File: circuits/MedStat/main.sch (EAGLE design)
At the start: 13 parts, among them U1 BLE113-VISUAL-A, U2 MMA8452Q

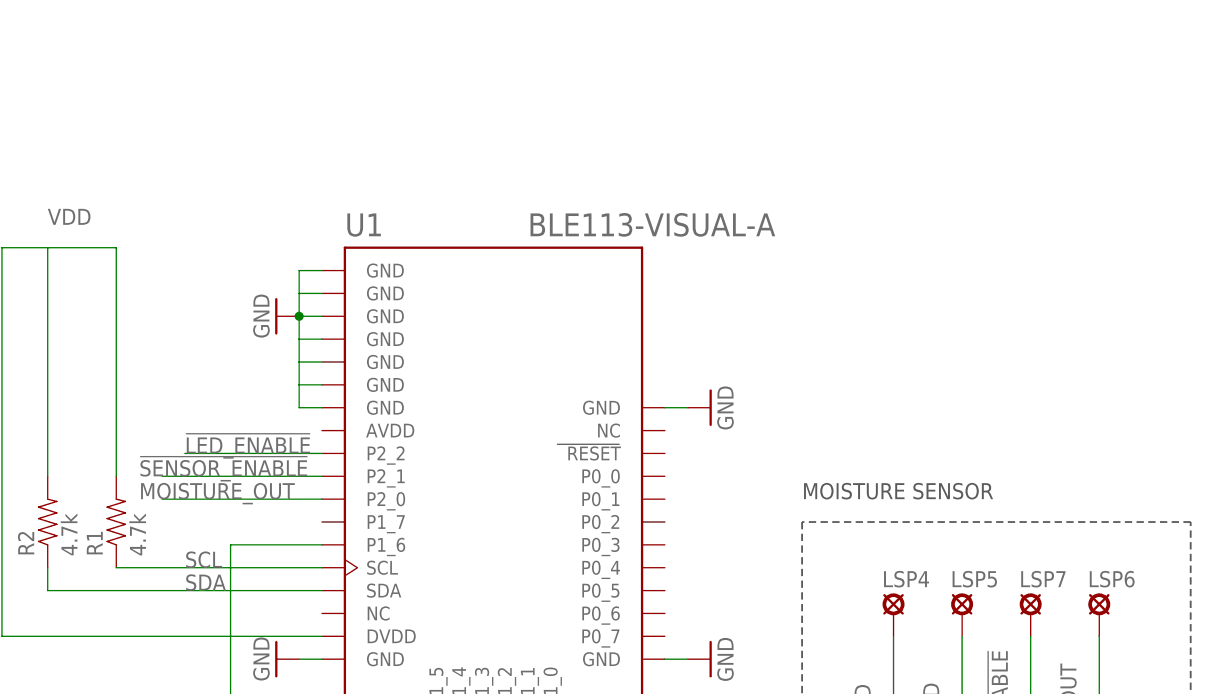
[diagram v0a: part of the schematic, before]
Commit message: Added pulse sensor ports
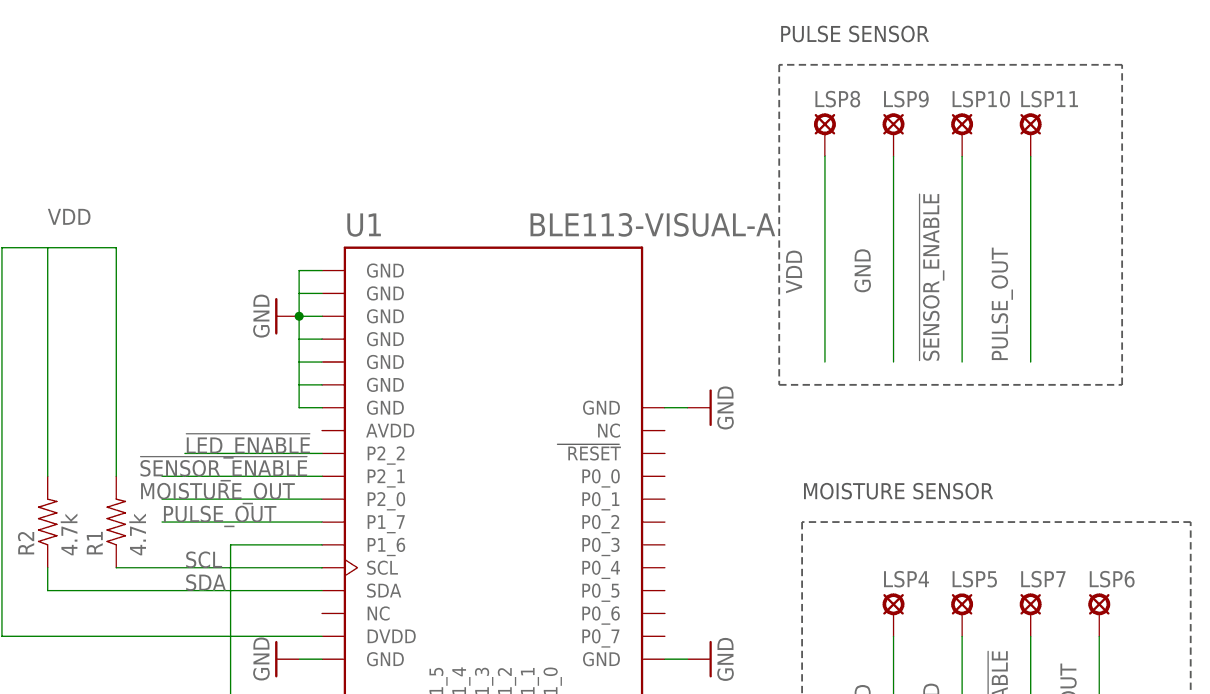
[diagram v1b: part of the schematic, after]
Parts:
- added LSP10, LSP11, LSP8, LSP9: LSP10, solpad:LSP10
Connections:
- new net PULSE_OUT: LSP11.MP, U1.P1_7
- net !SENSOR_ENABLE: now also LSP10.MP
- net GND: now also LSP9.MP
- net VDD: now also LSP8.MP
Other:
- note added: "PULSE SENSOR"
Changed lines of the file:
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@@
 <part name="LSP6" library="solpad" deviceset="LSP10" device=""/>
 <part name="LSP7" library="solpad" deviceset="LSP10" device=""/>
+<part name="LSP8" library="solpad" deviceset="LSP10" device=""/>
+<part name="LSP9" library="solpad" deviceset="LSP10" device=""/>
+<part name="LSP10" library="solpad" deviceset="LSP10" device=""/>
+<part name="LSP11" library="solpad" deviceset="LSP10" device=""/>
 </parts>
 <sheets>
@@
 <wire x1="76.2" y1="-2.54" x2="33.02" y2="-2.54" width="0.2032" layer="97" style="shortdash"/>
 <text x="33.02" y="0" size="1.778" layer="97">MOISTURE SENSOR</text>
+<wire x1="30.48" y1="48.26" x2="30.48" y2="12.7" width="0.2032" layer="97" style="shortdash"/>
+<wire x1="30.48" y1="12.7" x2="68.58" y2="12.7" width="0.2032" layer="97" style="shortdash"/>
+<wire x1="68.58" y1="12.7" x2="68.58" y2="48.26" width="0.2032" layer="97" style="shortdash"/>
+<wire x1="68.58" y1="48.26" x2="30.48" y2="48.26" width="0.2032" layer="97" style="shortdash"/>
+<text x="30.48" y="50.8" size="1.778" layer="97">PULSE SENSOR</text>
 </plain>
 <instances>
@@
 <instance part="LSP6" gate="1" x="66.04" y="-12.7"/>
 <instance part="LSP7" gate="1" x="58.42" y="-12.7"/>
+<instance part="LSP8" gate="1" x="35.56" y="40.64"/>
+<instance part="LSP9" gate="1" x="43.18" y="40.64"/>
+<instance part="LSP10" gate="1" x="50.8" y="40.64"/>
+<instance part="LSP11" gate="1" x="58.42" y="40.64"/>
 </instances>
 <busses>
@@
 <label x="48.26" y="-25.4" size="1.778" layer="95" rot="R90"/>
 </segment>
+<segment>
+<pinref part="LSP9" gate="1" pin="MP"/>
+<wire x1="43.18" y1="38.1" x2="43.18" y2="15.24" width="0.2032" layer="91"/>
+<label x="40.64" y="22.86" size="1.778" layer="95" rot="R90"/>
+</segment>
 </net>
 <net name="SDA" class="0">
@@
 <label x="40.64" y="-25.4" size="1.778" layer="95" rot="R90"/>
 </segment>
+<segment>
+<pinref part="LSP8" gate="1" pin="MP"/>
+<wire x1="35.56" y1="38.1" x2="35.56" y2="15.24" width="0.2032" layer="91"/>
+<label x="33.02" y="22.86" size="1.778" layer="95" rot="R90"/>
+</segment>
 </net>
 <net name="!LED_ENABLE" class="0">
@@
 <label x="-40.64" y="2.54" size="1.778" layer="95"/>
 </segment>
+<segment>
+<pinref part="LSP10" gate="1" pin="MP"/>
+<wire x1="50.8" y1="38.1" x2="50.8" y2="15.24" width="0.2032" layer="91"/>
+<label x="48.26" y="15.24" size="1.778" layer="95" rot="R90"/>
+</segment>
 </net>
 <net name="MOISTURE_OUT" class="0">
@@
 </segment>
 </net>
+<net name="PULSE_OUT" class="0">
+<segment>
+<pinref part="LSP11" gate="1" pin="MP"/>
+<wire x1="58.42" y1="38.1" x2="58.42" y2="15.24" width="0.2032" layer="91"/>
+<label x="55.88" y="15.24" size="1.778" layer="95" rot="R90"/>
+</segment>
+<segment>
+<pinref part="U1" gate="G$1" pin="P1_7"/>
+<wire x1="-20.32" y1="-2.54" x2="-38.1" y2="-2.54" width="0.2032" layer="91"/>
+<label x="-38.1" y="-2.54" size="1.778" layer="95"/>
+</segment>
+</net>

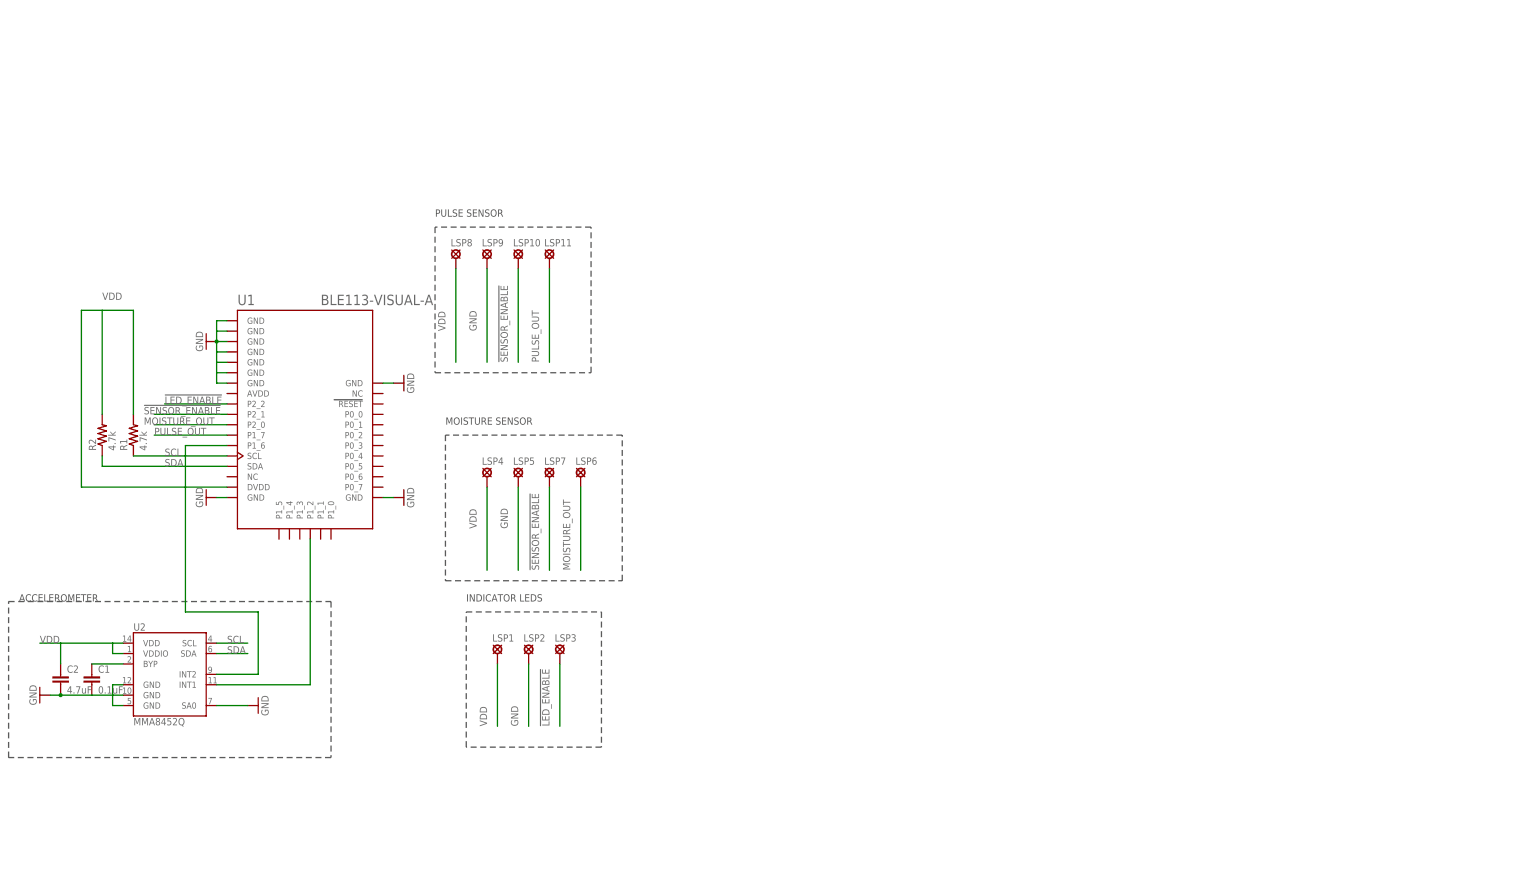
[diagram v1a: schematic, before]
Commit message: Integrated EPD driver to main schematic.
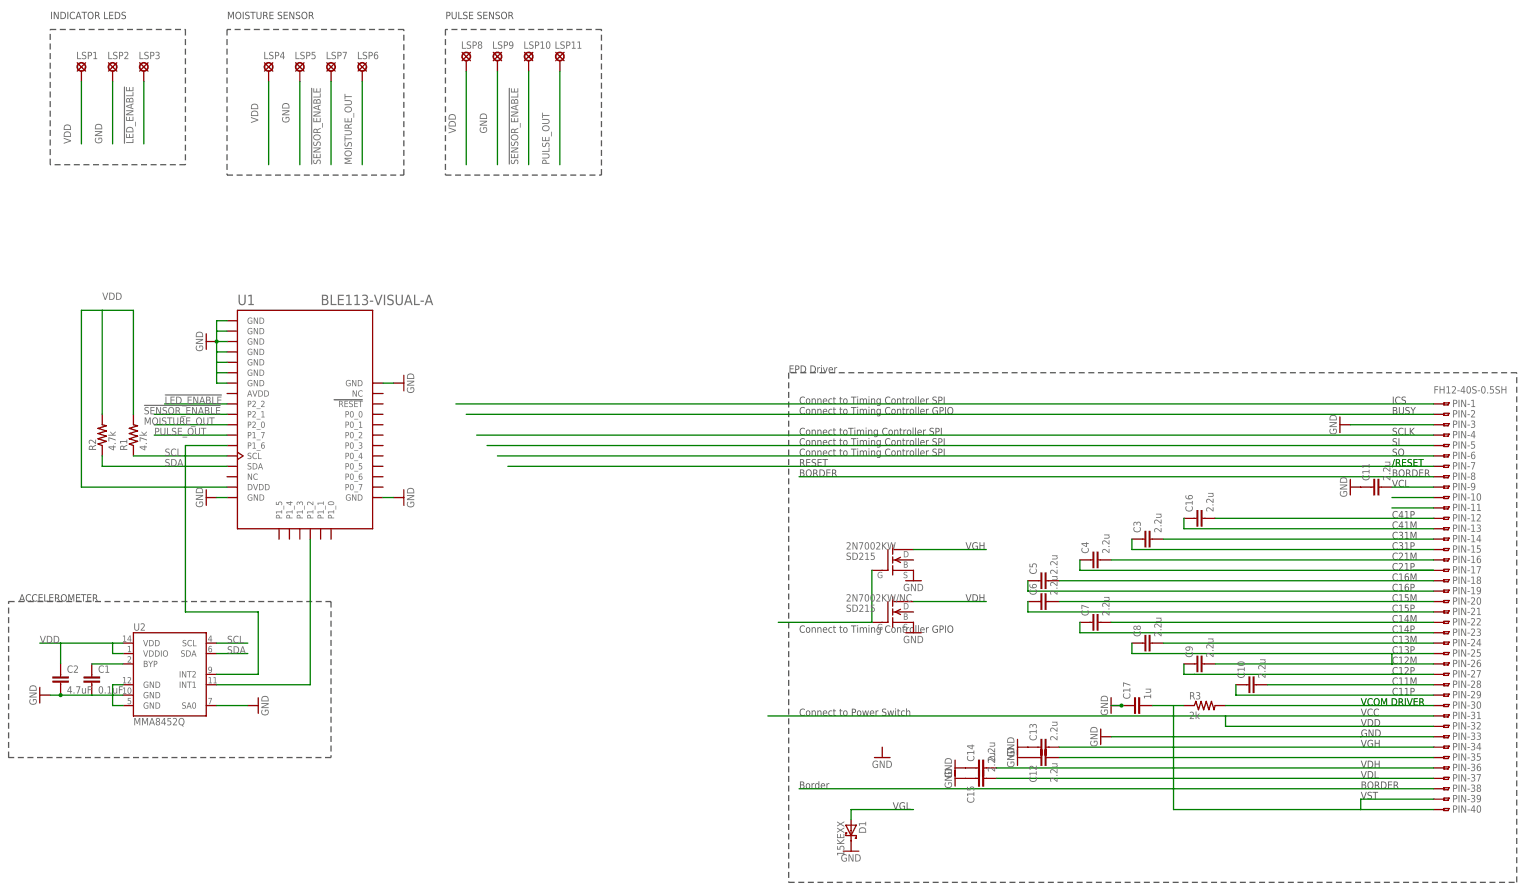
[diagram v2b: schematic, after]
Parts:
- added 2N7002KW, 2N7002KW/NC: SD215, transistor-fet:SD215
- added C10, C11, C12, C13, C14, C15, C16, C3, C4, C5, C6, C7, C8, C9: 2.2u, SparkFun-Capacitors:CAP0603-CAP
- added C17: 1u, SparkFun-Capacitors:CAP0603-CAP
- added D1: 15KEXX, diode:15KEXX
- added PIN: FH12-40S-0.5SH, con-hirose:FH12-40S-0.5SH
- added R3: 2k, SparkFun-Passives:RESISTOR0402-RES
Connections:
- new net ICS: PIN-1.1
- new net N$1: PIN-4.1
- new net N$10: PIN-10.1
- new net N$11: PIN-11.1
- new net N$12: C16.2, PIN-12.1
- new net N$13: C16.1, PIN-13.1
- new net N$14: C3.2, PIN-14.1
- new net N$15: C3.1, PIN-15.1
- new net N$16: C4.2, PIN-16.1
- new net N$17: C4.1, PIN-17.1
- new net N$18: C5.2, PIN-18.1
- new net N$19: C5.1, PIN-19.1
- new net N$2: PIN-2.1
- new net N$20: C6.2, PIN-20.1
- new net N$21: C6.1, PIN-21.1
- new net N$22: C7.2, PIN-22.1
- new net N$23: C7.1, PIN-23.1
- new net N$24: C8.2, PIN-24.1
- new net N$25: C8.1, C9.2, PIN-25.1
- new net N$26: PIN-26.1
- new net N$27: PIN-27.1
- new net N$28: C10.2, PIN-28.1
- new net N$29: C10.1, PIN-29.1
- new net N$30: PIN-30.1, R3.2
- new net N$31: PIN-31.1
- new net N$32: PIN-32.1
- new net N$33: PIN-33.1
- new net N$34: C12.2, PIN-34.1
- new net N$35: C13.2, PIN-35.1
- new net N$36: C14.2, PIN-36.1
- new net N$37: PIN-38.1
- new net N$38: C15.2, PIN-37.1
- new net N$39: PIN-8.1
- new net N$40: C17.2, PIN-39.1, PIN-40.1, R3.1
- new net N$41: 2N7002KW/NC.D
- new net N$42: 2N7002KW.D
- new net N$43: 2N7002KW.G, 2N7002KW/NC.G
- new net N$44: D1.A
- new net N$47: C9.1
- new net N$5: PIN-5.1
- new net N$6: PIN-6.1
- new net N$8: PIN-7.1
- new net N$9: C11.2, PIN-9.1
- net GND: now also 2N7002KW.S, 2N7002KW/NC.S, C11.1, C12.1, C13.1, C14.1, C15.1, C17.1, D1.C, PIN-3.1
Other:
- note added: "/RESET"
- note added: "BORDER"
- note added: "BUSY"
- note added: "Border"
- note added: "C11M"
- note added: "C11P"
- note added: "C12M"
- note added: "C12P"
- note added: "C13M"
- note added: "C13P"
- note added: "C14M"
- note added: "C14P"
- note added: "C15M"
- note added: "C15P"
- note added: "C16M"
- note added: "C16P"
- note added: "C21M"
- note added: "C21P"
- note added: "C31M"
- note added: "C31P"
- note added: "C41M"
- note added: "C41P"
- note added: "Connect to Power Switch"
- note added: "Connect to Timing Controller GPIO"
- note added: "Connect to Timing Controller SPI"
- note added: "Connect toTiming Controller SPI"
- note added: "EPD Driver"
- note added: "GND"
- note added: "ICS"
- note added: "RESET"
- note added: "SCLK"
- note added: "SI"
- note added: "SO"
- note added: "VCC"
- note added: "VCL"
- note added: "VCOM DRIVER"
- note added: "VDD"
- note added: "VDH"
- note added: "VDL"
- note added: "VGH"
- note added: "VGL"
- note added: "VST"
- moved on the sheet: LSP1, LSP10, LSP11, LSP2, LSP3, LSP4, LSP5, LSP6, LSP7, LSP8, LSP9

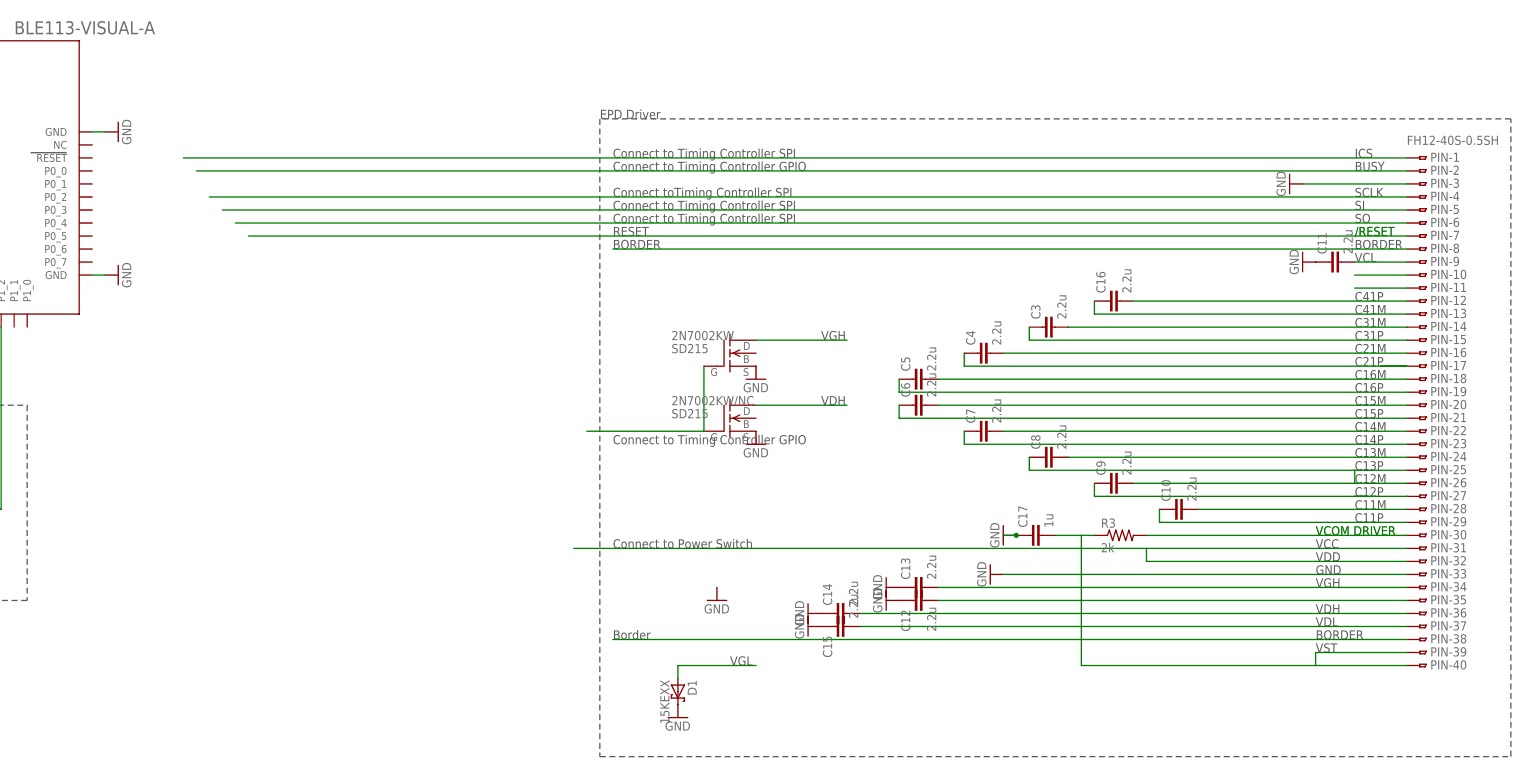
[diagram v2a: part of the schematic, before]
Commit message: Integrated EPD into main schematic.
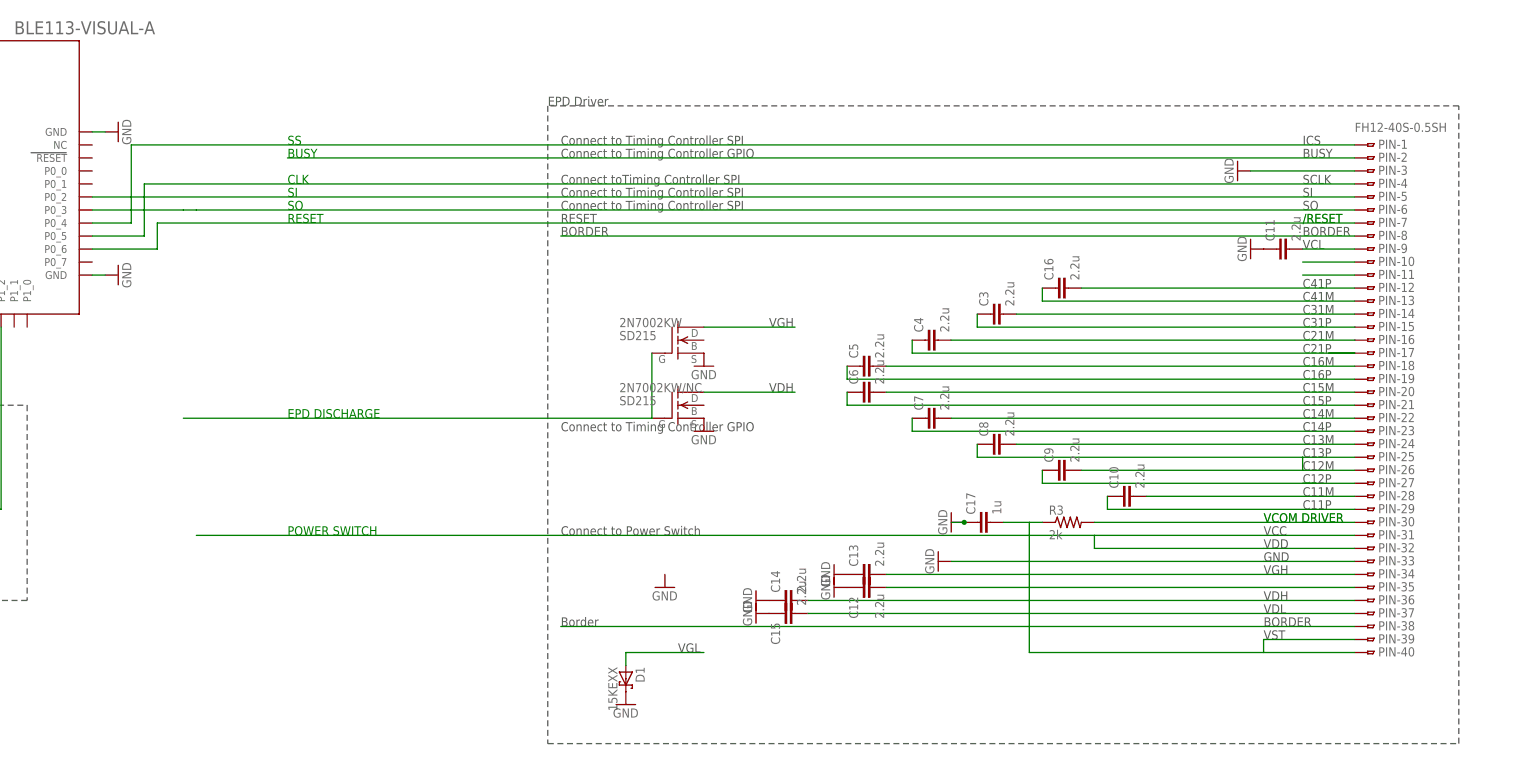
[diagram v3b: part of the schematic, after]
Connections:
- removed net ICS: PIN-1.1
- new net N$46: PIN-1.1, U1.P0_4
- net N$1: now also U1.P0_5
- net N$5: now also U1.P0_2
- net N$6: now also U1.P0_3
- net N$8: now also U1.P0_6
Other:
- note added: "CLK"
- note added: "EPD DISCHARGE"
- note added: "POWER SWITCH"
- note added: "SS"
- moved on the sheet: 2N7002KW, 2N7002KW/NC, C10, C11, C12, C13, C14, C15, C16, C17, C3, C4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
